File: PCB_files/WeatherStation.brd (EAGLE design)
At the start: 100 x 55 mm, 86 parts, among them CN1 S2B-PH-SM4, J1_RAIN RJ11, J2_WIND RJ11, Q1 SI2333DDS, Q2 BSS138, Q3 SI2333DDS, Q4 NC/SI2333DDS, Q5 BSS138, Q6 BSS138, Q7 NC/SI2333DDS, Q8 NC/BSS138, Q9 NC/SI2333DDS, U1 INA219BIDCNT, U3 SN74AUP2G14DCKR

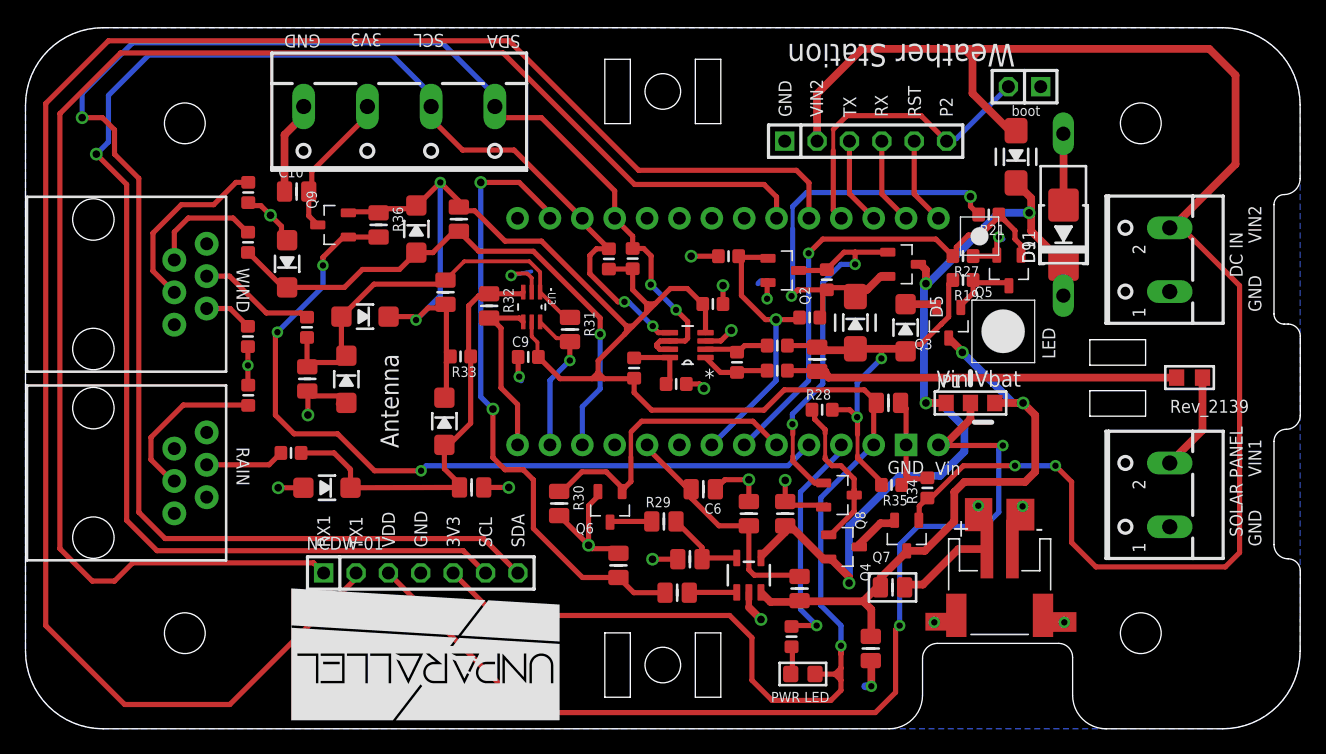
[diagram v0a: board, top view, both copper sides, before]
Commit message: Update the repository structure;  Update BOM list; Add/update assembly files; Add link in readme file
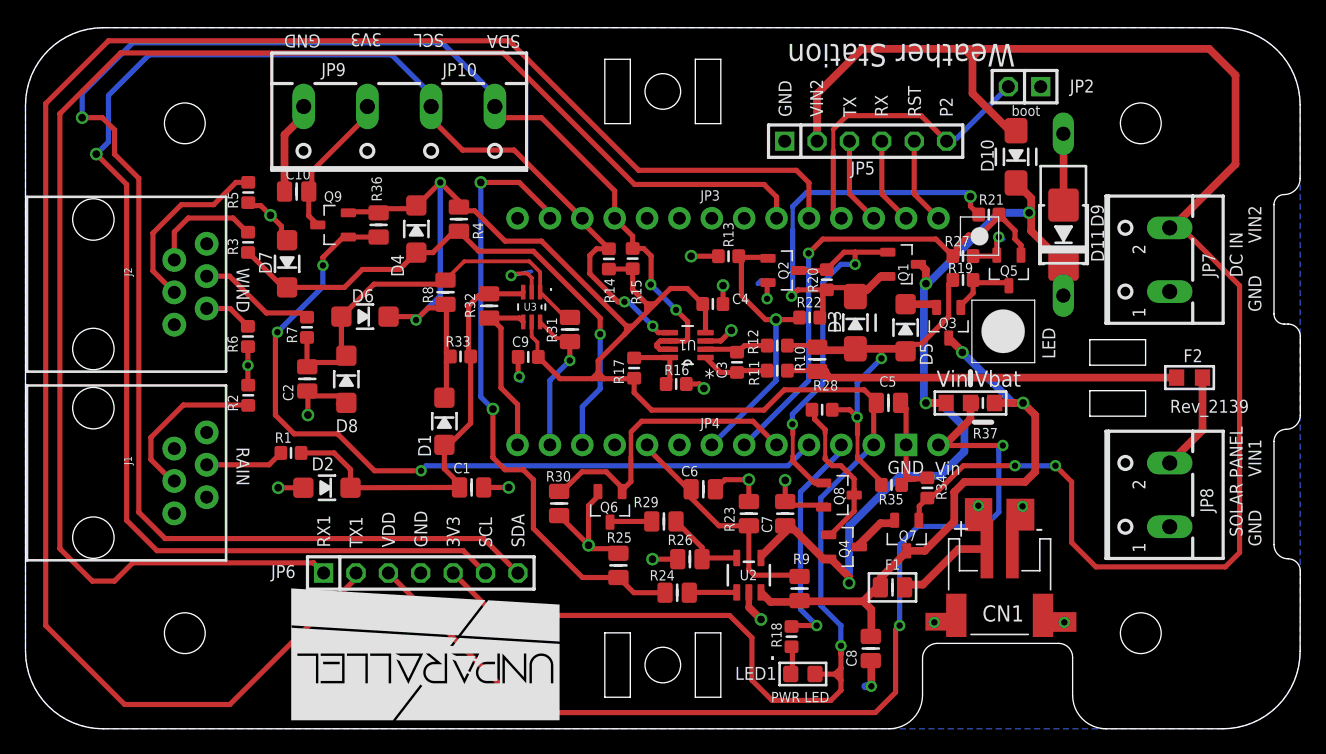
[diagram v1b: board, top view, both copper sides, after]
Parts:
- added R37: 0R, rcl_imp:R0603
- D10, D3: value RFN2LAM4STFTR/SS14L -> RFN2LAM4STFTR
- LED1: value (none) -> Green_LED
- Q9: value NC/SI2333DDS -> SI2333DDS
- R16: value CC/10k -> 0R
- R8: value 220k -> 22k
- U2: value (none) -> MCP73831T
- renumbered DC_IN to JP7, J1_RAIN to J1, J2_WIND to J2, NCDW-01 to JP6, NCDW-06 to JP5, SENSOR1 to JP9, SOLAR_POWER to JP8
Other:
- board text added: "."
- board text added: "JP10"
- board text added: "JP3"
- board text added: "JP4"
- board text removed: "Antenna"

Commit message: Updated Weather Station files
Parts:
- added C11, C12, C13: 100n, rcl_imp:C0603
- added D12: SS14L, diode:SUB_SMA_PROTO
- added J3: XMEGA-PDI, atmel-xmega_imp:HDR-MA02-3P_P0.05_FABIO
- added R38, R39: 10k, rcl_imp:R0603
- added R40: 0R, rcl_imp:R0603
- added U$3: ATXMEGAE5, atmel-xmega_imp:TQFP32_PROTO_SLIM
- CN1: device adafruit_edit:JST-PH-2-SMT-RA -> adafruit:JST-PH-2-SMT-RA_OK
- F2: device ptc-ntc:R0805 -> ptc-ntc:R0603/R0805_PROTO_SLIM
- JP6: device pinhead:1X07 -> pinhead:1X08
- R26, R30, R31, R32, R4, R8: device rcl_imp:R0603/R0805_PROTO_SLIM -> rcl_imp:R0603
- moved R25 1.75 mm to (48.3, 12.8)
- moved C9 1.25 mm to (38.3, 28.7), turned to 270 degrees
- moved JP6 1.25 mm to (29.8, 12.2)
- moved U$1 1.19 mm to (40.7, 11.0)
- moved R24 0.95 mm to (52.1, 10.7)
- moved R33 0.50 mm to (34.0, 28.7)
- moved R31 0.48 mm to (43.2, 31.2)
- moved D2 0.46 mm to (23.9, 19.3)
- moved D1 0.29 mm to (33.0, 23.9)
- moved R26 0.16 mm to (52.1, 13.5)
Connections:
- removed net WSPD_INV: R31.2, U$2.P$16, U3.6
- new net N$14: R40.2, U3.6
- new net UART_!SS: JP6.1, U$3.12
- new net WD_!RST: J3.3, R38.2, U$3.8
- new net WD_PDI: J3.2, U$3.7
- new net WSPD_INV_: C13.1, R31.2, R40.1
- new net WSPD_INV_PULSE: C13.2, D12.C, R39.1, U$2.P$16, U$3.10
- net +3V3: now also C11.2, C12.2, JP6.6, R38.1, U$3.17, U$3.32; no longer JP6.5
- net BAT: now also CN1.3
- net BAT_FUSE: now also R37.2
- net GND: now also C11.1, C12.1, CN1.4, D12.A, J3.1, JP6.5, R39.2, U$3.1, U$3.18; no longer JP6.4
- net RAIN_INV: now also U$3.9
- net RST: now also U$3.11
- net RX1: now also JP6.2, U$3.13; no longer JP6.1
- net SCL: now also JP6.7, U$3.15; no longer JP6.6
- net SDA: now also JP6.8, U$3.16; no longer JP6.7
- net TX1: now also JP6.3, U$3.14; no longer JP6.2
- net VIN: now also JP6.4, R37.1; no longer JP6.3
- net WDIR: now also U$3.5
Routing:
- net RST: track 6.85 -> 86.3 mm, vias 0 -> 4
- net WSPD_INV_PULSE: track 0.00 -> 37.9 mm, vias 0 -> 4
- net GND: track 91.1 -> 123.5 mm
- net +3V3: track 176.1 -> 208.3 mm
- net WD_PDI: track 0.00 -> 25.6 mm, vias 0 -> 1
- net UART_!SS: track 0.00 -> 22.8 mm
- net RX1: track 121.3 -> 141.5 mm
- net WDIR: track 44.3 -> 63.0 mm
- net RAIN_INV: track 13.8 -> 29.7 mm, vias 0 -> 2
- net WD_!RST: track 0.00 -> 15.8 mm, vias 0 -> 1
- net SCL: track 124.1 -> 139.3 mm, vias 3 -> 4
- net WSPD_INV: track 11.7 -> 0.00 mm, vias 1 -> 0
- net TX1: track 141.7 -> 153.3 mm
- net SDA: track 134.5 -> 144.9 mm, vias 3 -> 4
- net BAT: track 7.82 -> 17.9 mm, vias 0 -> 2
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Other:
- board text added: "Rev_2202"
- board text removed: "Rev_2139"
